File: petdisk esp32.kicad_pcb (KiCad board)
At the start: 2 copper layers, 75 x 37.8 mm, 32 parts, among them J1 Conn_01x08, J3 Micro_SD_Card_Det2, J31 PET_IEEE_M, J4 PET_IEEE, Q1 BSS138, Q2 BSS138, Q3 BSS138, Q4 BSS138, Q5 BSS138, U1 ESP32-WROOM-32D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

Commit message: Added readme, images, pdf, gerber (zip).
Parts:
- added REF**: OSHW-Logo2_9.8x8mm_SilkScreen, Library:OSHW-Logo2_9.8x8mm_SilkScreen, B.Cu at (126.2, 74.8)
- J3: value Micro_SD_Card_Det2 -> Hanbo TS-013
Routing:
- net /ports/NDAC: track 54.6 -> 64.2 mm, vias 3 -> 2
- net /ports/DIO4: track 56.6 -> 55.2 mm
- net VCC: track 154.5 -> 155.2 mm, vias 1 -> 0
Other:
- board text added: "Based on github.com /bitfixer/petdisk-max (esp32) /svenpetersen1965/PET-IEEE-488-Extension /yo5ptd/petdisk-esp32 2025.06.27"
- board text removed: "Based on github.com/ bitfixer/petdisk-max (esp32) svenpetersen1965/PET-IEEE-488-Extension yo5ptd/petdisk esp32 2025.06.27"

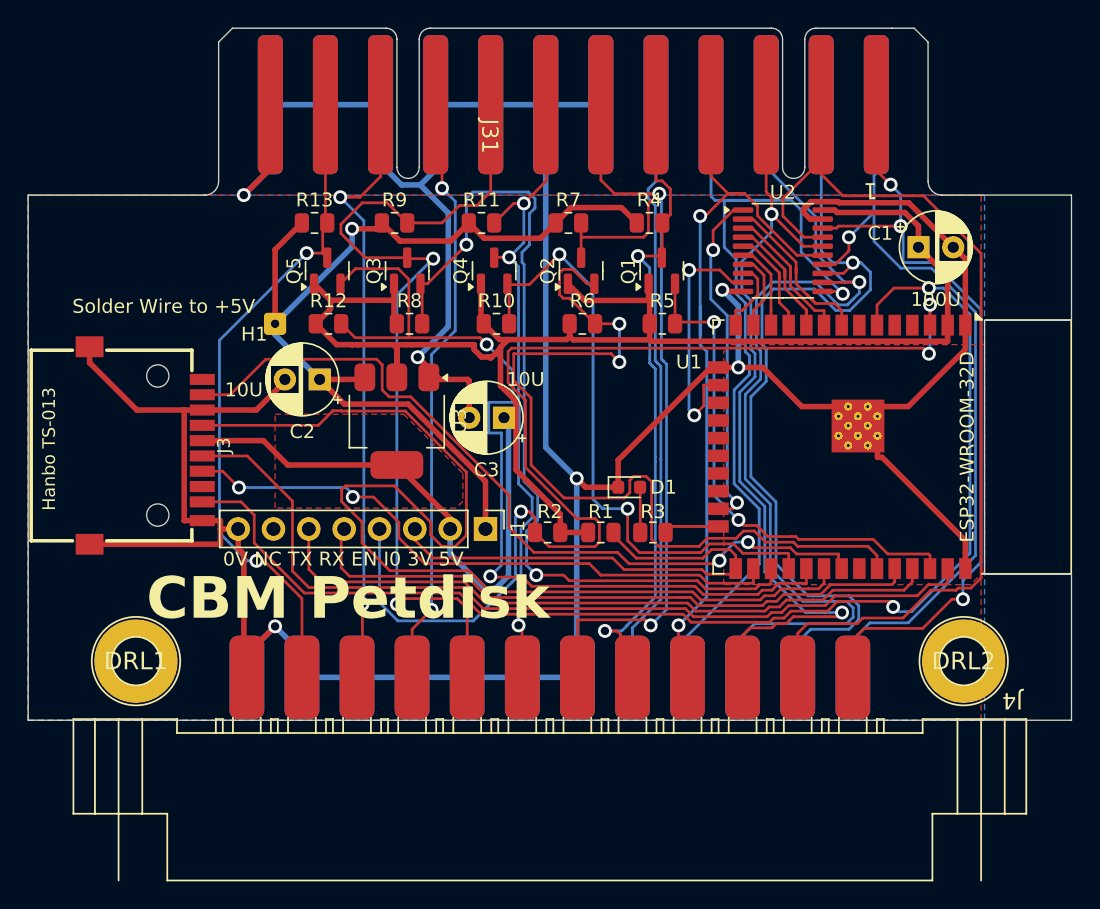
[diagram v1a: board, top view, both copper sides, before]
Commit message: Files ordered from JLCPCB.
connector silkscreen fix
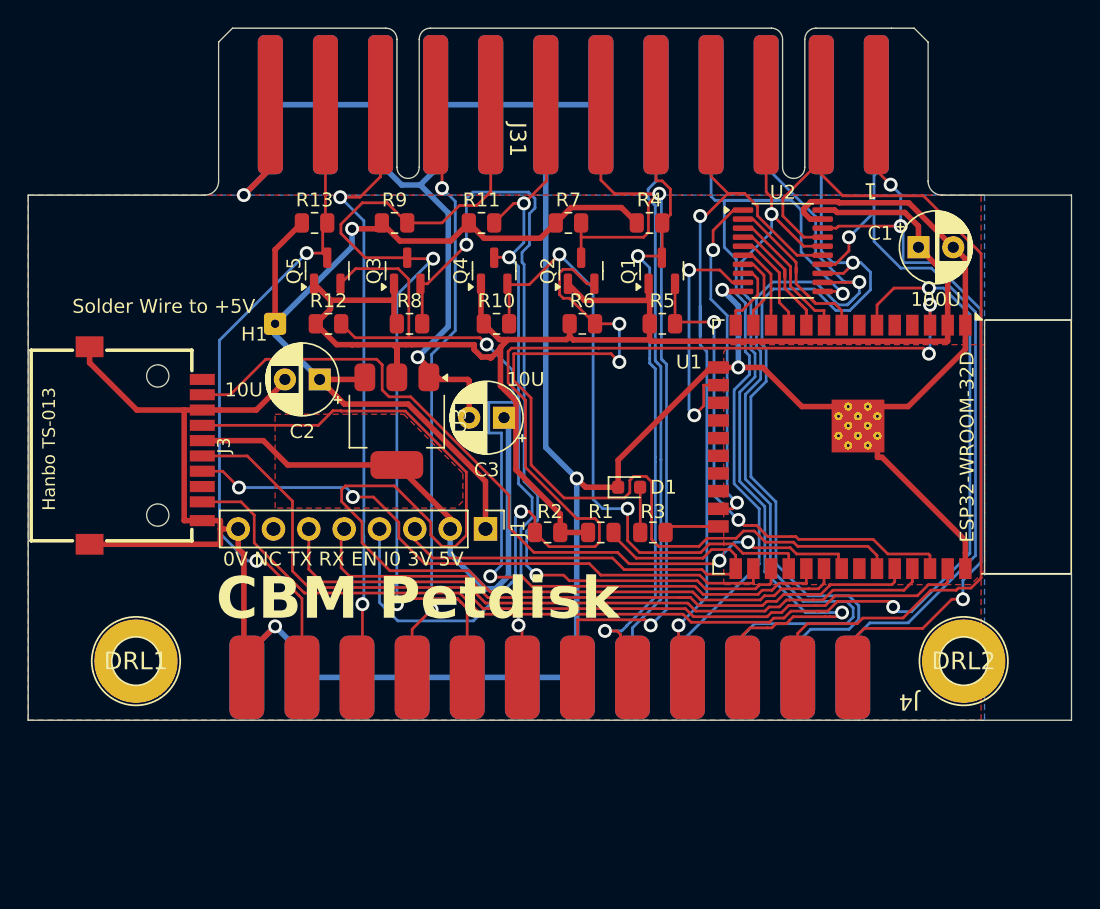
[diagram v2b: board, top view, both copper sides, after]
